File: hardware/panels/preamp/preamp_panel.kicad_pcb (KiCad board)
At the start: 2 copper layers, 93 x 93 mm, 274 parts, among them J1 I/O, J2 Conn 1, J3 Conn 2, Q1 2SC3324, Q2 2SC3324, U1 TLV170DBV

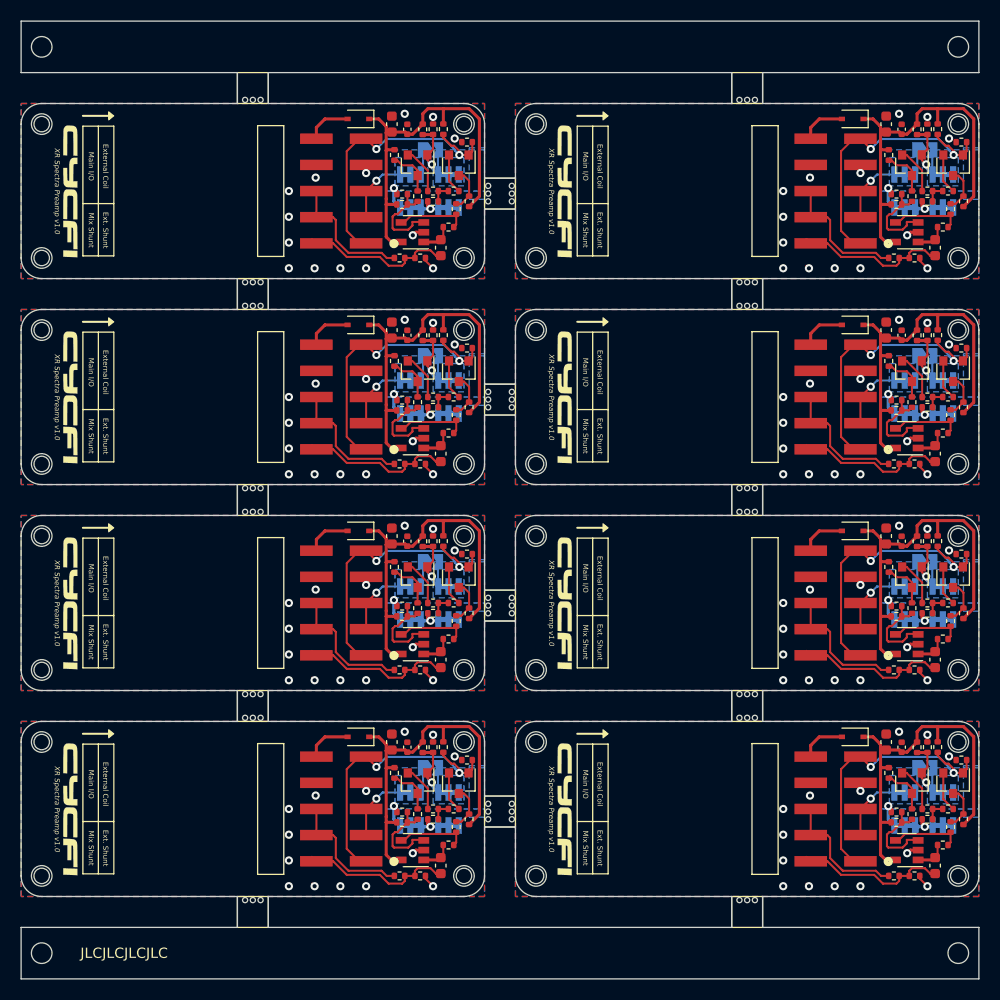
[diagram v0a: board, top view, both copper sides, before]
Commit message: Preamp, Tone Block, Passive, and Bobbin Panel updates
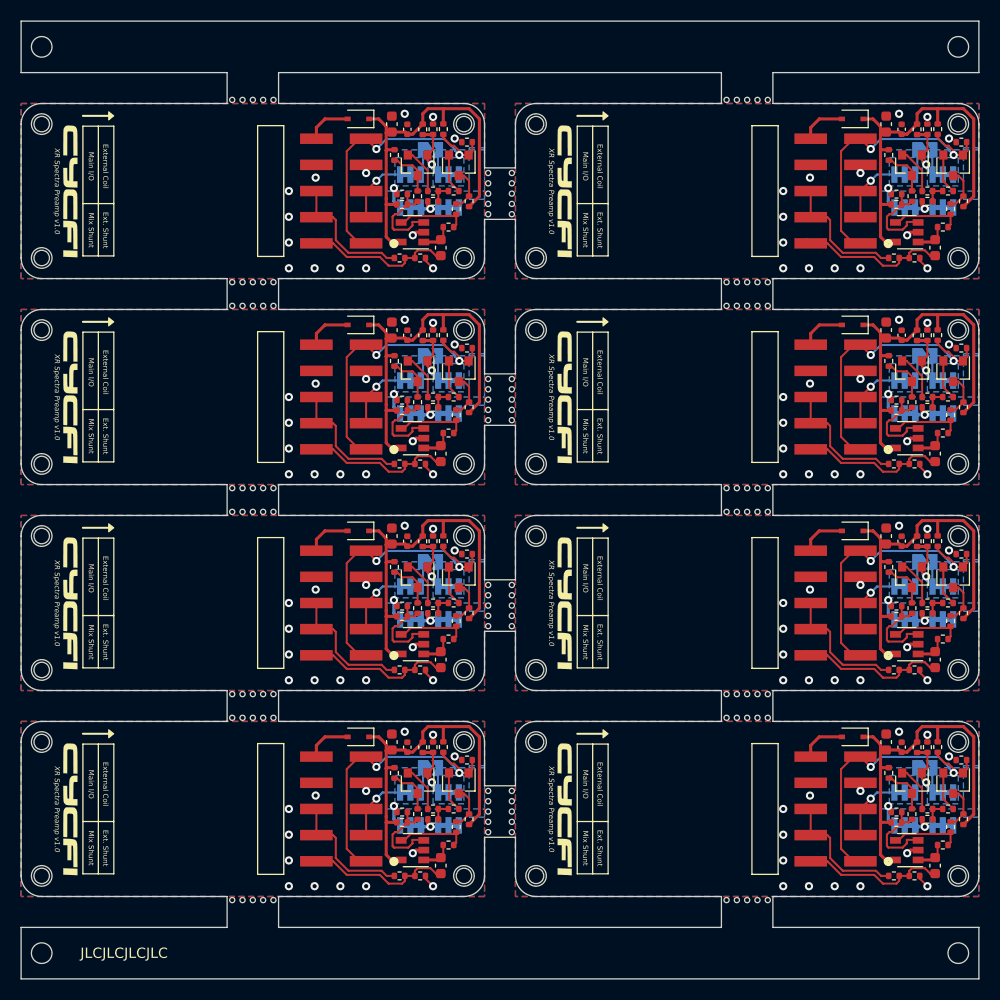
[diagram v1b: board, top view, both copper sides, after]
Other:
- outline, holes or cut-outs redrawn
